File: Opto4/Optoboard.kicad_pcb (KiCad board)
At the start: 2 copper layers, 68 x 35 mm, 40 parts, among them J1 S1 Connector, J2 S2 Connector, J3 S3 Connector, J4 S4 Connector, J5 Conn_01x06, Q1 IRLR024NPBF, U1 6N135, U2 6N135, U3 6N135, U4 6N135

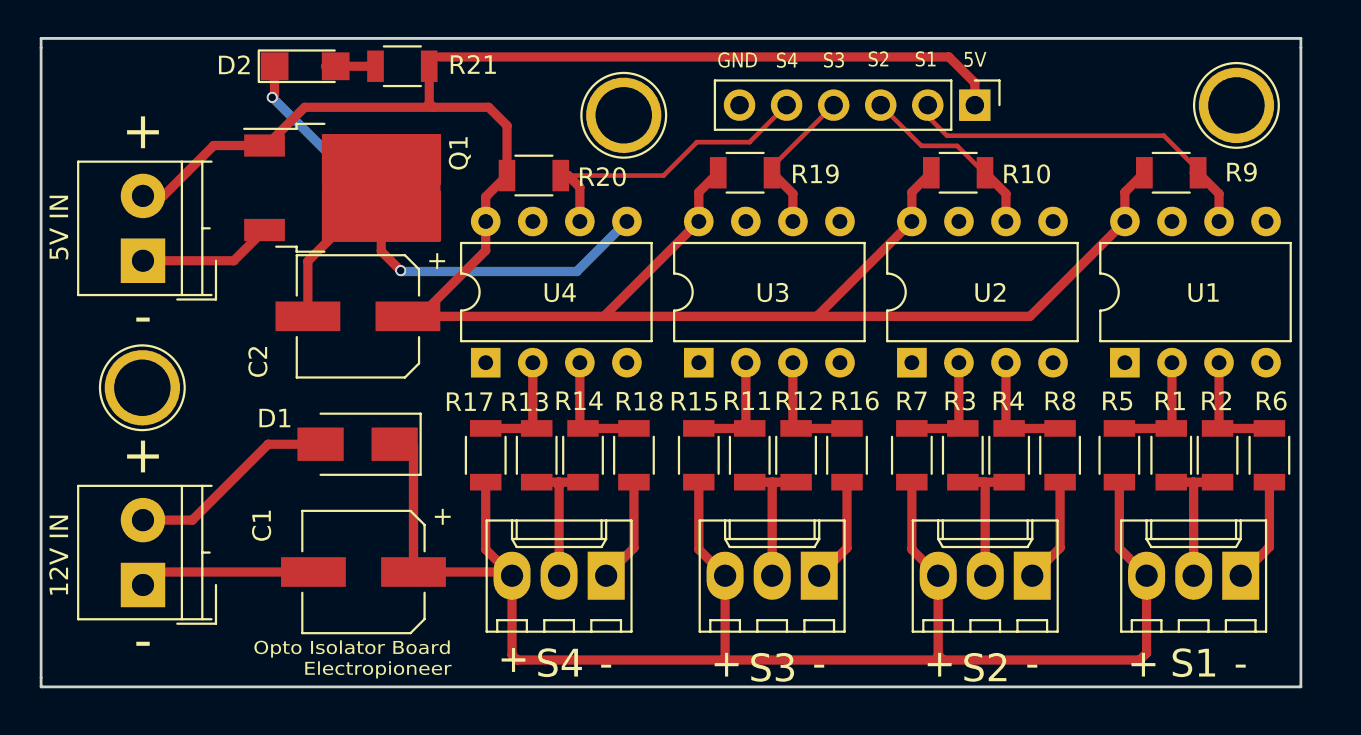
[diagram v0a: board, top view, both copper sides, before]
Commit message: Added opto4 and opto6 updated images
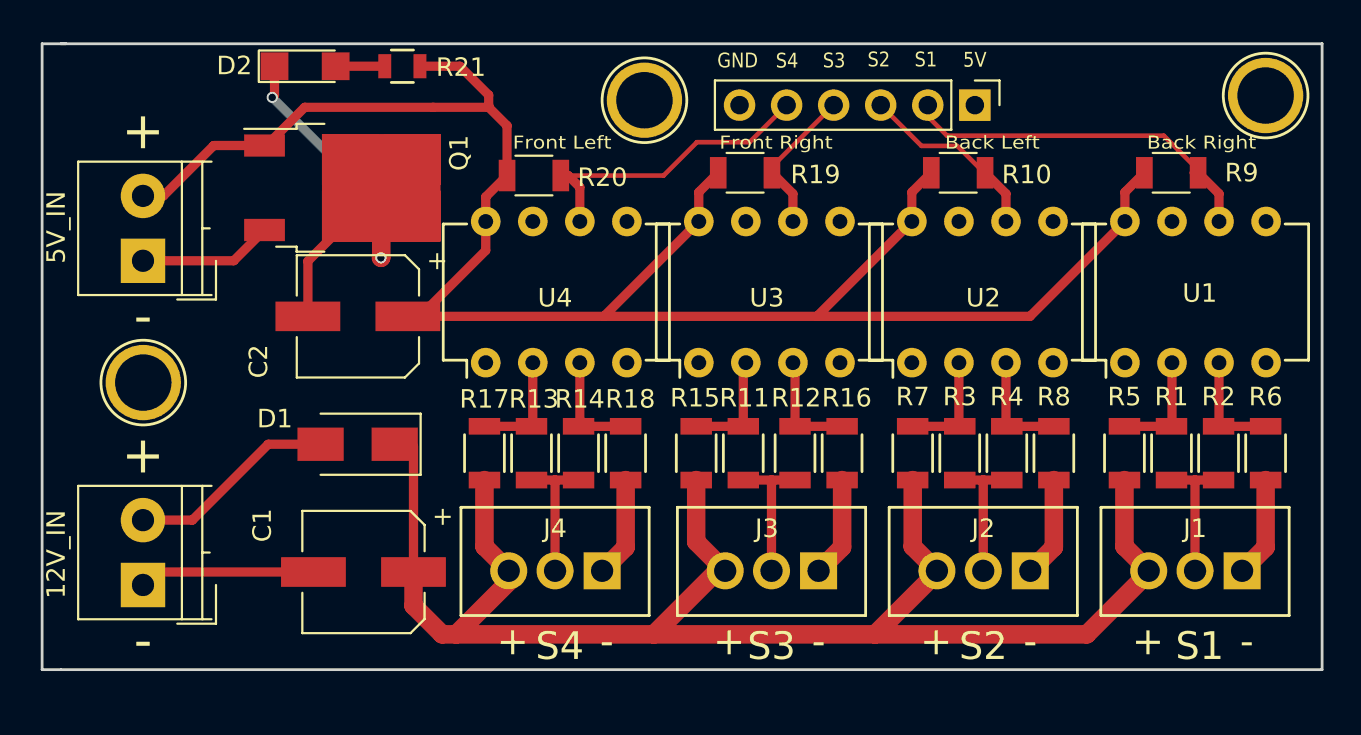
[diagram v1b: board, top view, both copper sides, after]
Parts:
- removed the REF** at (164.5, 109.9)
- removed the REF** at (223.5, 94.6)
- removed the REF** at (190.4, 95.1)
- added REF**: 1pin, Connect:1pin, F.Cu at (164.5, 109.6)
- added REF**: 1pin, Connect:1pin, F.Cu at (225.1, 94.1)
- added REF**: 1pin, Connect:1pin, F.Cu at (191.6, 94.3)
- 12V_IN: renamed from 12V IN
- 5V_IN: renamed from 5V IN
- J1, J2, J3, J4: footprint Connectors_Molex:Molex_KK-6410-03_03x2.54mm_Straight -> Connect:Wafer_Vertical10x5.8x7RM2.5-3
- R21: footprint Resistors_SMD:R_1206 -> Resistors_SMD:R_0805
- moved R18 0.46 mm to (190.6, 113.4)
- moved R11 0.37 mm to (196.9, 113.4)
- moved R8 0.35 mm to (213.7, 113.4)
- moved J4 0.34 mm to (189.3, 119.7)
- moved R13 0.30 mm to (185.5, 113.4)
- moved R5 0.30 mm to (217.5, 113.4)
- moved R16 0.29 mm to (202.2, 113.4)
- moved J2 0.28 mm to (212.4, 119.7)
- moved J1 0.27 mm to (223.8, 119.7)
- moved J3 0.27 mm to (201.0, 119.7)
- moved R14 0.27 mm to (188.0, 113.4)
- moved R6 0.23 mm to (225.1, 113.4)
- moved R3 0.20 mm to (208.6, 113.4)
- moved R15 0.18 mm to (194.4, 113.4)
- moved R4 0.17 mm to (211.1, 113.4)
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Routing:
- net +5V: track 132.4 -> 104.4 mm
- net GND: track 68.3 -> 52.8 mm
- net Net-(J2-Pad2): track 8.75 -> 7.59 mm
- net Net-(J4-Pad2): track 7.95 -> 7.44 mm
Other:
- board size 68 x 35 mm -> 69.1 x 33.8 mm
- board text added: "Back Left"
- board text added: "Back Right"
- board text added: "Front Left"
- board text added: "Front Right"
- board text removed: "Opto Isolator Board Electropioneer"

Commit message: Changed some traces
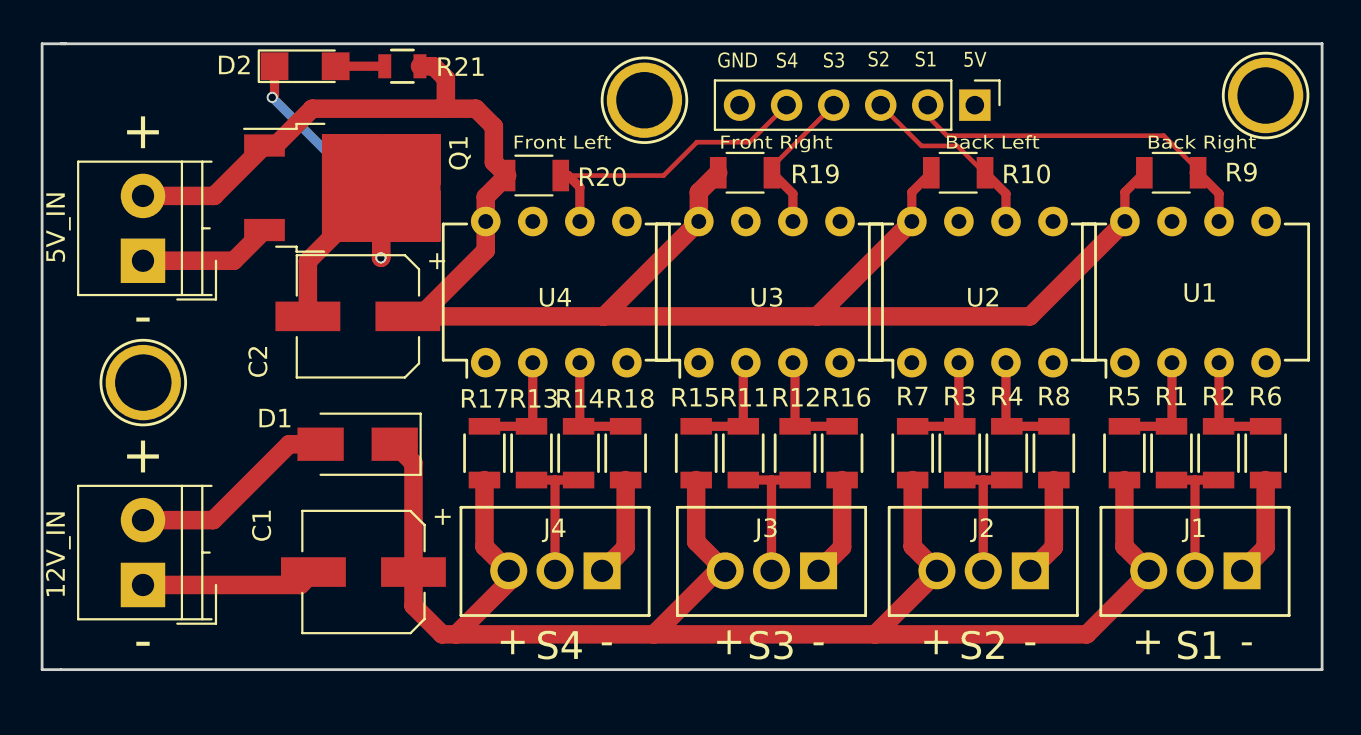
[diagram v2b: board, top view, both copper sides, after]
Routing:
- net +5V: track 104.4 -> 146.4 mm
- net GND: track 52.8 -> 59.4 mm
- net +12V: track 88.0 -> 88.5 mm
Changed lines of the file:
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@@
     (links 77)
     (no_connects 1)
-    (area 158.979799 91.212599 228.217801 125.144601)
+    (area 140.419087 85.6436 238.9368 127.453572)
     (thickness 1.6)
     (drawings 39)
-    (tracks 151)
+    (tracks 164)
     (zones 0)
     (modules 40)
@@
   )
   (setup
-    (last_trace_width 0.25)
+    (last_trace_width 1)
     (user_trace_width 0.25)
     (user_trace_width 0.5)
@@
     (effects (font (size 2 2) (thickness 0.3)))
   )
+  (segment (start 173.4 106) (end 173.4 103.02) (width 1) (layer F.Cu) (net 1) (status 400000))
+  (segment (start 173.4 103.02) (end 177.36 99.06) (width 1) (layer F.Cu) (net 1) (status 800000))
+  (segment (start 164.5 120.5) (end 173 120.5) (width 1) (layer F.Cu) (net 1))
+  (segment (start 173 120.5) (end 173.7 119.8) (width 1) (layer F.Cu) (net 1))
   (segment (start 177.36 99.06) (end 177.36 102.8274) (width 1) (layer F.Cu) (net 1))
   (via (at 177.3428 102.8446) (size 0.6) (drill 0.4) (layers F.Cu B.Cu) (net 1))
@@
   (via (at 171.4754 94.1832) (size 0.6) (drill 0.4) (layers F.Cu B.Cu) (net 1))
   (segment (start 171.6 94.0586) (end 171.4754 94.1832) (width 0.5) (layer F.Cu) (net 1))
-  (segment (start 173.4 106) (end 173.4 103.02) (width 0.5) (layer F.Cu) (net 1))
   (segment (start 173.4 103.02) (end 177.36 99.06) (width 0.5) (layer F.Cu) (net 1))
-  (segment (start 173.7 119.8) (end 165.2 119.8) (width 0.5) (layer F.Cu) (net 1))
   (segment (start 165.2 119.8) (end 164.5 120.5) (width 0.5) (layer F.Cu) (net 1))
   (segment (start 173.4 106) (end 173.48 106) (width 0.5) (layer F.Cu) (net 1))
-  (segment (start 164.5 117) (end 167.1625 117) (width 0.5) (layer F.Cu) (net 2))
-  (segment (start 171.2595 112.903) (end 174.0855 112.903) (width 0.5) (layer F.Cu) (net 2))
-  (segment (start 167.1625 117) (end 171.2595 112.903) (width 0.5) (layer F.Cu) (net 2))
+  (segment (start 164.5 117) (end 168.2928 117) (width 1) (layer F.Cu) (net 2))
+  (segment (start 172.3898 112.903) (end 174.0855 112.903) (width 1) (layer F.Cu) (net 2))
+  (segment (start 168.2928 117) (end 172.3898 112.903) (width 1) (layer F.Cu) (net 2))
+  (segment (start 179.1 119.8) (end 179.1 113.9175) (width 1) (layer F.Cu) (net 3))
+  (segment (start 179.1 113.9175) (end 178.0855 112.903) (width 1) (layer F.Cu) (net 3))
   (segment (start 207.3548 119.7356) (end 207.3548 119.8226) (width 1) (layer F.Cu) (net 3))
   (segment (start 207.3548 119.8226) (end 204.0128 123.1646) (width 1) (layer F.Cu) (net 3))
@@
   (segment (start 178.0855 112.903) (end 179.0065 112.903) (width 0.5) (layer F.Cu) (net 3))
   (segment (start 179.0065 112.903) (end 179.1 112.9965) (width 0.5) (layer F.Cu) (net 3))
-  (segment (start 179.1 112.9965) (end 179.1 119.8) (width 0.5) (layer F.Cu) (net 3))
-  (segment (start 179.45 92.5) (end 181.6032 92.5) (width 0.5) (layer F.Cu) (net 4))
-  (segment (start 183.1594 94.0562) (end 183.1594 94.5896) (width 0.5) (layer F.Cu) (net 4))
-  (segment (start 183.1594 94.5896) (end 183.1594 94.7166) (width 0.5) (layer F.Cu) (net 4))
-  (segment (start 181.6032 92.5) (end 183.1594 94.0562) (width 0.5) (layer F.Cu) (net 4))
-  (segment (start 178.8 106) (end 179.4452 106) (width 0.5) (layer F.Cu) (net 4))
+  (segment (start 200.88 106) (end 212.38 106) (width 1) (layer F.Cu) (net 4))
+  (segment (start 212.38 106) (end 217.5 100.88) (width 1) (layer F.Cu) (net 4) (status 800000))
+  (segment (start 189.3316 106) (end 200.88 106) (width 1) (layer F.Cu) (net 4))
+  (segment (start 200.88 106) (end 206 100.88) (width 1) (layer F.Cu) (net 4) (status 800000))
+  (segment (start 194.5 100.88) (end 194.5 99.3) (width 1) (layer F.Cu) (net 4) (status 400000))
+  (segment (start 194.5 99.3) (end 195.55 98.25) (width 1) (layer F.Cu) (net 4) (status 800000))
+  (segment (start 178.8 106) (end 189.3316 106) (width 1) (layer F.Cu) (net 4) (status 400000))
+  (segment (start 189.3316 106) (end 189.38 106) (width 1) (layer F.Cu) (net 4))
+  (segment (start 189.38 106) (end 194.5 100.88) (width 1) (layer F.Cu) (net 4) (status 800000))
+  (segment (start 183 100.88) (end 183 99.55) (width 1) (layer F.Cu) (net 4) (status 400000))
+  (segment (start 183 99.55) (end 184.15 98.4) (width 1) (layer F.Cu) (net 4) (status 800000))
+  (segment (start 178.8 106) (end 179.4452 106) (width 1) (layer F.Cu) (net 4) (status C00000))
+  (segment (start 179.4452 106) (end 183 102.4452) (width 1) (layer F.Cu) (net 4) (status 400000))
+  (segment (start 183 102.4452) (end 183 100.88) (width 1) (layer F.Cu) (net 4) (status 800000))
+  (segment (start 179.45 92.5) (end 180.1808 92.5) (width 1) (layer F.Cu) (net 4))
+  (segment (start 180.848 93.1672) (end 180.848 94.7928) (width 1) (layer F.Cu) (net 4))
+  (segment (start 180.1808 92.5) (end 180.848 93.1672) (width 1) (layer F.Cu) (net 4))
+  (segment (start 171.06 96.78) (end 171.6472 96.78) (width 1) (layer F.Cu) (net 4))
+  (segment (start 171.6472 96.78) (end 173.6344 94.7928) (width 1) (layer F.Cu) (net 4))
+  (segment (start 183.4388 97.6888) (end 184.15 98.4) (width 1) (layer F.Cu) (net 4))
+  (segment (start 183.4388 95.758) (end 183.4388 97.6888) (width 1) (layer F.Cu) (net 4))
+  (segment (start 182.4736 94.7928) (end 183.4388 95.758) (width 1) (layer F.Cu) (net 4))
+  (segment (start 173.6344 94.7928) (end 180.848 94.7928) (width 1) (layer F.Cu) (net 4))
+  (segment (start 180.848 94.7928) (end 182.4736 94.7928) (width 1) (layer F.Cu) (net 4))
+  (segment (start 164.5 99.5) (end 168.34 99.5) (width 1) (layer F.Cu) (net 4))
+  (segment (start 168.34 99.5) (end 171.06 96.78) (width 1) (layer F.Cu) (net 4))
   (segment (start 179.4452 106) (end 183 102.4452) (width 0.5) (layer F.Cu) (net 4))
   (segment (start 183 102.4452) (end 183 100.88) (width 0.5) (layer F.Cu) (net 4))
   (segment (start 171.06 96.78) (end 171.1646 96.78) (width 0.5) (layer F.Cu) (net 4))
-  (segment (start 171.1646 96.78) (end 173.228 94.7166) (width 0.5) (layer F.Cu) (net 4))
-  (segment (start 184.15 95.7072) (end 184.15 98.4) (width 0.5) (layer F.Cu) (net 4))
-  (segment (start 183.1594 94.7166) (end 184.15 95.7072) (width 0.5) (layer F.Cu) (net 4))
-  (segment (start 173.228 94.7166) (end 180.1622 94.7166) (width 0.5) (layer F.Cu) (net 4))
-  (segment (start 180.1622 94.7166) (end 183.1594 94.7166) (width 0.5) (layer F.Cu) (net 4))
   (segment (start 164.5 99.5) (end 165.5998 99.5) (width 0.5) (layer F.Cu) (net 4))
-  (segment (start 165.5998 99.5) (end 168.3198 96.78) (width 0.5) (layer F.Cu) (net 4))
-  (segment (start 168.3198 96.78) (end 171.06 96.78) (width 0.5) (layer F.Cu) (net 4))
-  (segment (start 200.88 106) (end 212.38 106) (width 0.5) (layer F.Cu) (net 4))
   (segment (start 212.38 106) (end 217.5 100.88) (width 0.5) (layer F.Cu) (net 4))
   (segment (start 189.38 106) (end 200.88 106) (width 0.5) (layer F.Cu) (net 4))
   (segment (start 200.88 106) (end 206 100.88) (width 0.5) (layer F.Cu) (net 4))
-  (segment (start 178.8 106) (end 189.38 106) (width 0.5) (layer F.Cu) (net 4))
   (segment (start 189.38 106) (end 194.5 100.88) (width 0.5) (layer F.Cu) (net 4))
   (segment (start 217.5 100.88) (end 217.5 99.3) (width 0.5) (layer F.Cu) (net 4))
@@
   (segment (start 206 100.88) (end 206 99.3) (width 0.5) (layer F.Cu) (net 4))
   (segment (start 206 99.3) (end 207.05 98.25) (width 0.5) (layer F.Cu) (net 4))
-  (segment (start 194.5 100.88) (end 194.5 99.3) (width 0.5) (layer F.Cu) (net 4))
   (segment (start 194.5 99.3) (end 195.55 98.25) (width 0.5) (layer F.Cu) (net 4))
-  (segment (start 183 100.88) (end 183 99.55) (width 0.5) (layer F.Cu) (net 4))
   (segment (start 183 99.55) (end 184.15 98.4) (width 0.5) (layer F.Cu) (net 4))
   (segment (start 221.2848 119.7356) (end 221.2848 114.8356) (width 0.5) (layer F.Cu) (net 5))
@@
   (segment (start 188.08 111.8664) (end 188.0108 111.9356) (width 0.5) (layer F.Cu) (net 20))
   (segment (start 174.9 92.5) (end 177.55 92.5) (width 0.5) (layer F.Cu) (net 21))
-  (segment (start 164.5 103) (end 169.4 103) (width 0.5) (layer F.Cu) (net 22))
-  (segment (start 169.4 103) (end 171.06 101.34) (width 0.5) (layer F.Cu) (net 22))
+  (segment (start 164.5 103) (end 169.4 103) (width 1) (layer F.Cu) (net 22))
+  (segment (start 169.4 103) (end 171.06 101.34) (width 1) (layer F.Cu) (net 22))
   (segment (start 164.5 103) (end 165.25 103) (width 0.5) (layer F.Cu) (net 22))
   (zone (net 1) (net_name GND) (layer B.Cu) (hatch edge 0.508)

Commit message: Added output files for both version
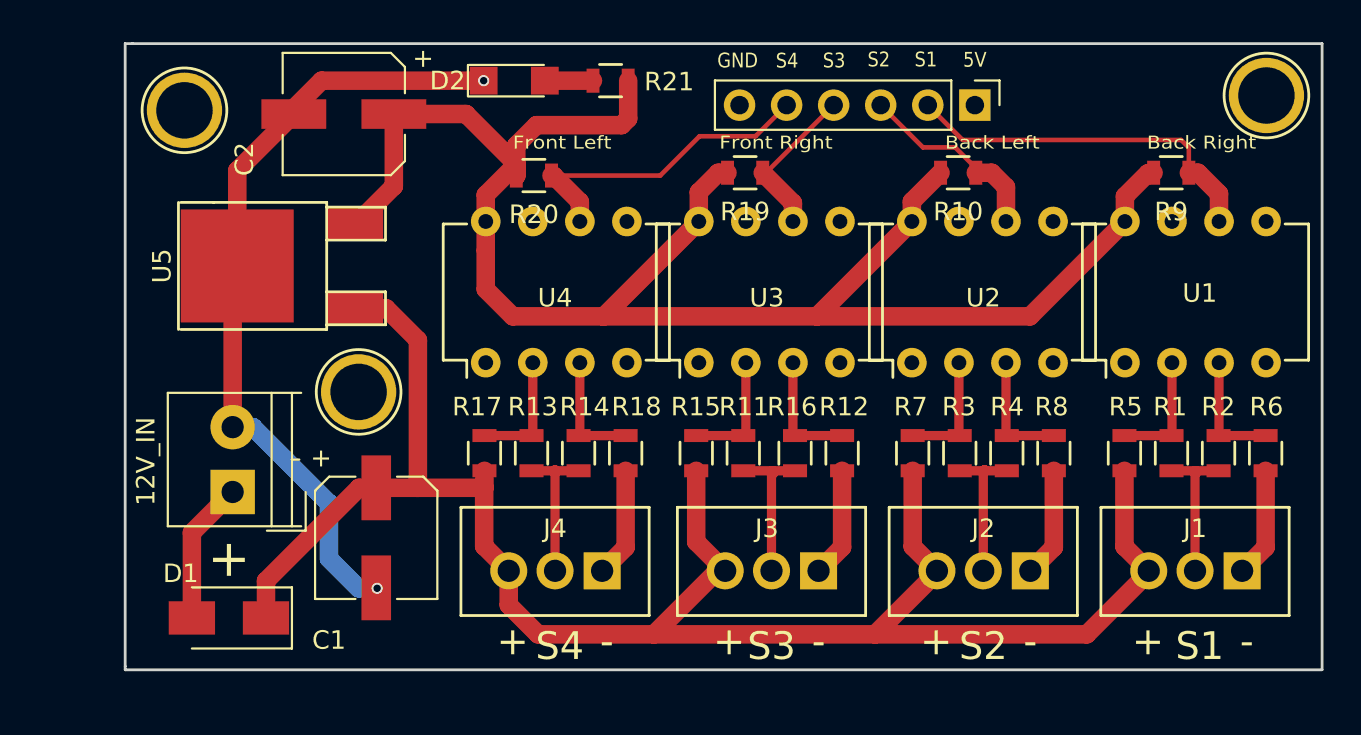
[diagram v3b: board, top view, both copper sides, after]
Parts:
- removed 5V_IN: Screw_Terminal_01x02, Connectors_Terminal_Blocks:TerminalBlock_4UCON_19963_02x3.5mm_Straight
- removed Q1: IRLR024NPBF, TO_SOT_Packages_SMD:TO-252-2
- removed the REF** at (164.5, 109.6)
- removed the REF** at (225.1, 94.1)
- removed the REF** at (191.6, 94.3)
- added REF**: 1pin, Connect:1pin, F.Cu at (176.1, 110.1)
- added REF**: 1pin, Connect:1pin, F.Cu at (166.7, 94.9)
- added REF**: 1pin, Connect:1pin, F.Cu at (225.1, 94.1)
- added U5: L7805, TO_SOT_Packages_SMD:TO-252-2Lead, F.Cu at (175.9, 103.3)
- R1, R10, R11, R12, R13, R14, R15, R16, R17, R18, R19, R2, R20, R3, R4, R5, R6, R7, R8, R9: footprint Resistors_SMD:R_1206 -> Resistors_SMD:R_0805
- moved D1 11.7 mm to (169.1, 122.3)
- moved D2 11.3 mm to (184.5, 93.3)
- moved R21 11.3 mm to (189.7, 93.3)
- moved C2 10.9 mm to (175.3, 95.1)
- moved 12V_IN 6.97 mm to (169.3, 115.5)
- moved C1 1.97 mm to (177.1, 118.0), turned to 270 degrees
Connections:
- 12V_IN pad 1: GND -> Net-(12V_IN1-Pad1)
- 12V_IN pad 2: Net-(12V_IN1-Pad2) -> GND
- D1 pad 2: Net-(12V_IN1-Pad2) -> Net-(12V_IN1-Pad1)
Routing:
- net +5V: track 146.4 -> 131.8 mm
- net +12V: track 88.5 -> 101.0 mm
- net Net-(12V_IN1-Pad2): track 11.3 -> 0.00 mm
- net GND: track 59.4 -> 70.2 mm
- net Net-(5V_IN1-Pad1): track 8.00 -> 0.00 mm
- net Net-(12V_IN1-Pad1): track 0.00 -> 7.71 mm
- net S1: track 20.0 -> 24.1 mm
- net Net-(R11-Pad1): track 6.03 -> 6.73 mm
- net Net-(J3-Pad2): track 7.84 -> 8.53 mm
- net Net-(J1-Pad2): track 7.59 -> 8.25 mm
- net Net-(R12-Pad1): track 6.02 -> 6.69 mm
- net Net-(J4-Pad2): track 7.44 -> 8.05 mm
- net S4: track 16.9 -> 17.4 mm
- net S3: track 8.13 -> 8.65 mm
- net Net-(J2-Pad2): track 7.59 -> 8.10 mm
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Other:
- board size 69.1 x 33.8 mm -> 64.6 x 33.8 mm
